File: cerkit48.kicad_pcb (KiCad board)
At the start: 2 copper layers, 251.5 x 128.3 mm, 104 parts, among them J1 I2C, SW1 SW_Push_Dual_x2, SW10 CherryMX, SW11 CherryMX, SW12 CherryMX, SW13 CherryMX, SW14 CherryMX, SW15 CherryMX, SW16 CherryMX, SW17 CherryMX, SW18 CherryMX, SW19 CherryMX, SW2 CherryMX, SW20 CherryMX, SW21 CherryMX, SW22 CherryMX, SW23 CherryMX, SW24 CherryMX, SW25 CherryMX, SW26 CherryMX, SW27 CherryMX, SW28 CherryMX, SW29 CherryMX, SW3 CherryMX, SW30 CherryMX, SW31 CherryMX, SW32 CherryMX, SW33 CherryMX, SW34 CherryMX, SW35 CherryMX, SW36 CherryMX, SW37 CherryMX, SW38 CherryMX, SW39 CherryMX, SW4 CherryMX, SW40 CherryMX, SW41 CherryMX, SW42 CherryMX, SW43 CherryMX, SW44 CherryMX, SW45 CherryMX, SW46 CherryMX, SW47 CherryMX, SW48 CherryMX, SW49 CherryMX, SW5 CherryMX, SW6 CherryMX, SW7 CherryMX, SW8 CherryMX, SW9 CherryMX, U1 proton_c

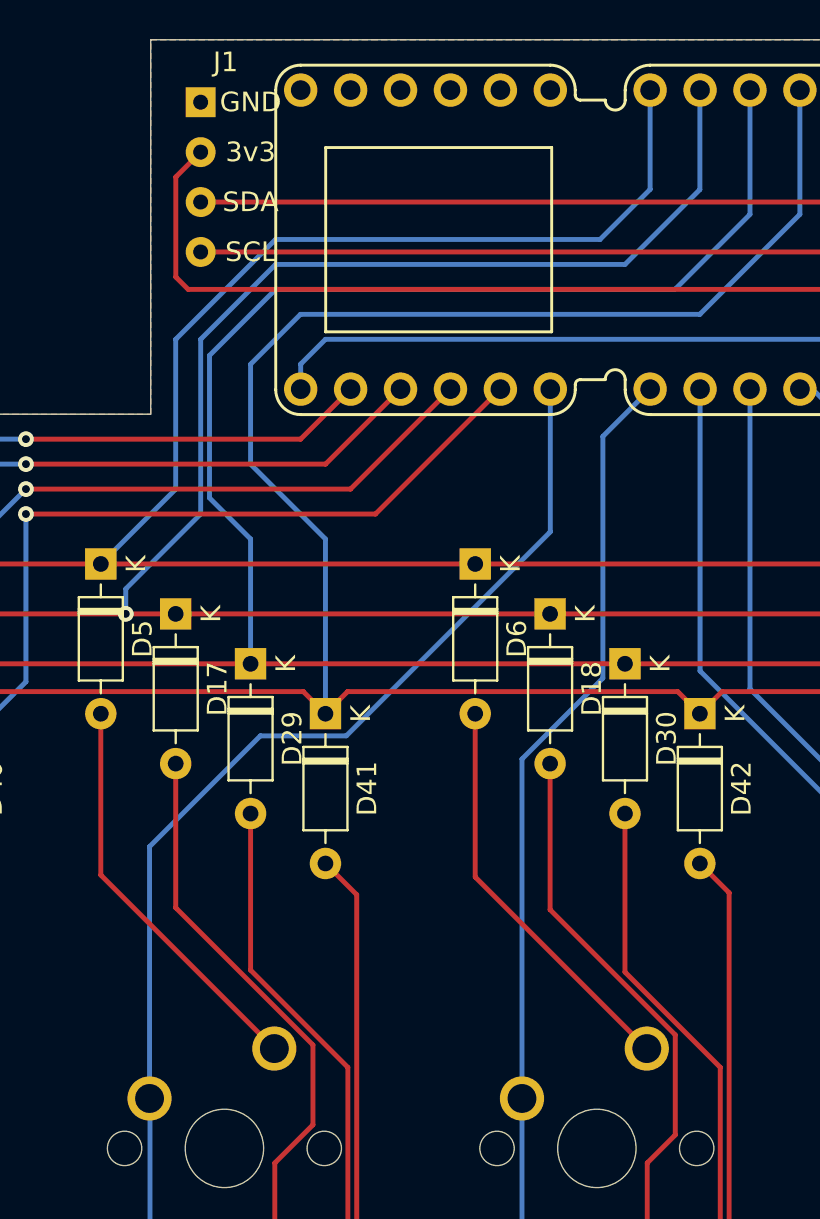
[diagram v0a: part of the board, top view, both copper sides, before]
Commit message: reworked back traces
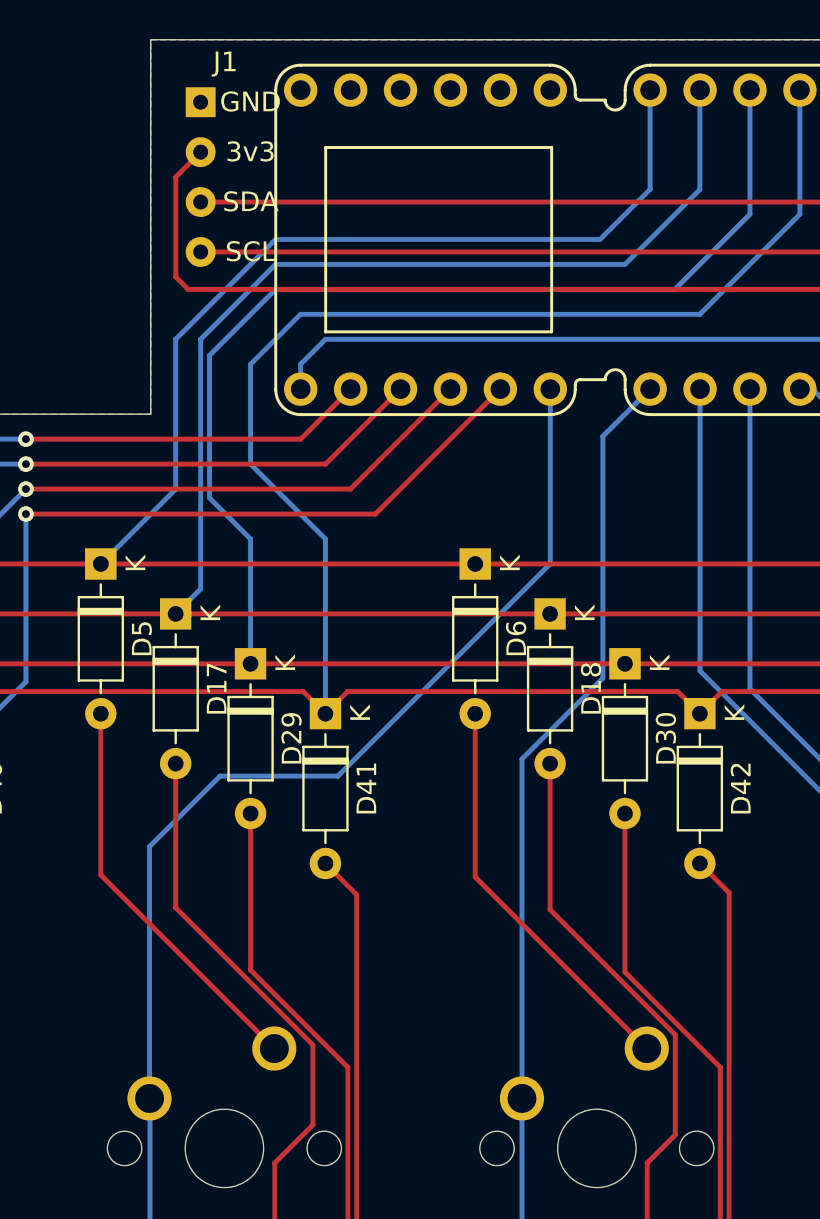
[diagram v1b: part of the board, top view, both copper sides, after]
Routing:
- net ROW1: track 258.7 -> 257.7 mm, vias 1 -> 0
- net COL4: track 104.3 -> 105.3 mm
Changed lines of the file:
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@@
     (thickness 1.6)
     (drawings 1054)
-    (tracks 478)
+    (tracks 475)
     (zones 0)
     (modules 104)
@@
   (segment (start 57.15 60.96) (end 36.83 60.96) (width 0.25) (layer F.Cu) (net 15))
   (segment (start 111.76 60.96) (end 95.25 60.96) (width 0.25) (layer F.Cu) (net 15))
-  (via (at 111.76 60.96) (size 0.8) (drill 0.4) (layers F.Cu B.Cu) (net 15))
-  (segment (start 114.3 57.15) (end 114.3 57.15) (width 0.25) (layer B.Cu) (net 15))
-  (segment (start 140.97 34.32) (end 140.98 34.31) (width 0.25) (layer B.Cu) (net 15))
-  (segment (start 140.97 39.37) (end 140.97 34.32) (width 0.25) (layer B.Cu) (net 15))
-  (segment (start 137.16 43.18) (end 140.97 39.37) (width 0.25) (layer B.Cu) (net 15))
-  (segment (start 111.76 59.69) (end 115.57 55.88) (width 0.25) (layer B.Cu) (net 15))
-  (segment (start 115.57 55.88) (end 115.57 46.99) (width 0.25) (layer B.Cu) (net 15))
-  (segment (start 111.76 60.96) (end 111.76 59.69) (width 0.25) (layer B.Cu) (net 15))
-  (segment (start 115.57 46.99) (end 119.38 43.18) (width 0.25) (layer B.Cu) (net 15))
-  (segment (start 119.38 43.18) (end 137.16 43.18) (width 0.25) (layer B.Cu) (net 15))
+  (segment (start 115.57 59.69) (end 114.3 60.96) (width 0.25) (layer B.Cu) (net 15))
+  (segment (start 115.57 46.99) (end 115.57 59.69) (width 0.25) (layer B.Cu) (net 15))
+  (segment (start 140.97 34.32) (end 140.97 39.37) (width 0.25) (layer B.Cu) (net 15))
+  (segment (start 140.98 34.31) (end 140.97 34.32) (width 0.25) (layer B.Cu) (net 15))
+  (segment (start 140.97 39.37) (end 137.16 43.18) (width 0.25) (layer B.Cu) (net 15))
+  (segment (start 137.16 43.18) (end 119.38 43.18) (width 0.25) (layer B.Cu) (net 15))
+  (segment (start 119.38 43.18) (end 115.57 46.99) (width 0.25) (layer B.Cu) (net 15))
   (segment (start 62.055655 102.033073) (end 62.055655 85.264345) (width 0.25) (layer F.Cu) (net 16))
   (segment (start 62.055655 85.264345) (end 63.5 83.82) (width 0.25) (layer F.Cu) (net 16))
@@
   (segment (start 112.948698 142.633493) (end 112.83523 142.746961) (width 0.25) (layer B.Cu) (net 62))
   (segment (start 112.948698 123.717779) (end 112.948698 142.633493) (width 0.25) (layer B.Cu) (net 62))
-  (segment (start 133.36 56.785002) (end 133.36 49.525) (width 0.25) (layer B.Cu) (net 62))
-  (segment (start 122.980001 67.165001) (end 133.36 56.785002) (width 0.25) (layer B.Cu) (net 62))
-  (segment (start 112.969212 72.805786) (end 118.609997 67.165001) (width 0.25) (layer B.Cu) (net 62))
-  (segment (start 118.609997 67.165001) (end 122.980001 67.165001) (width 0.25) (layer B.Cu) (net 62))
-  (segment (start 112.969212 85.617632) (end 112.969212 72.805786) (width 0.25) (layer B.Cu) (net 62))
+  (segment (start 112.969212 72.805786) (end 112.969212 85.617632) (width 0.25) (layer B.Cu) (net 62))
+  (segment (start 116.559998 69.215) (end 112.969212 72.805786) (width 0.25) (layer B.Cu) (net 62))
+  (segment (start 122.555 69.215) (end 116.559998 69.215) (width 0.25) (layer B.Cu) (net 62))
+  (segment (start 133.36 49.525) (end 133.36 58.41) (width 0.25) (layer B.Cu) (net 62))
+  (segment (start 133.36 58.41) (end 122.555 69.215) (width 0.25) (layer B.Cu) (net 62))
   (segment (start 131.957876 123.71475) (end 132.010576 123.66205) (width 0.25) (layer B.Cu) (net 63))
   (segment (start 131.957876 142.76019) (end 131.957876 123.71475) (width 0.25) (layer B.Cu) (net 63))

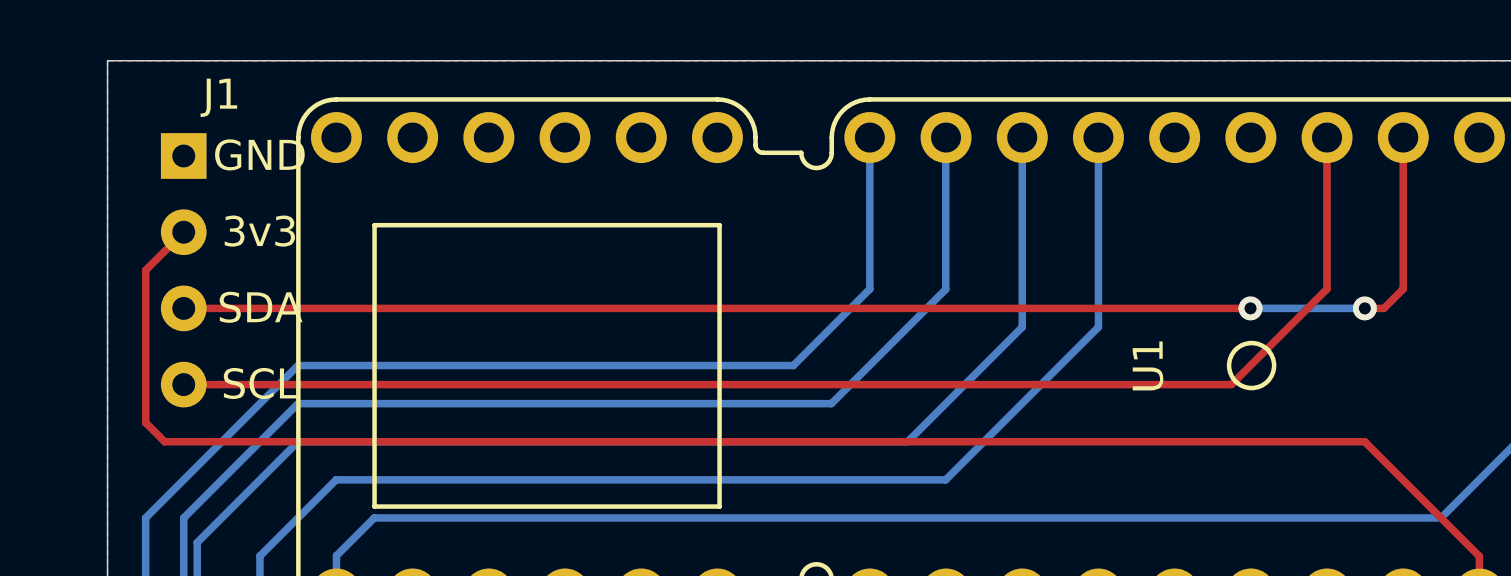
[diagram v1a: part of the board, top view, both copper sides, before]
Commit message: reworked front traces
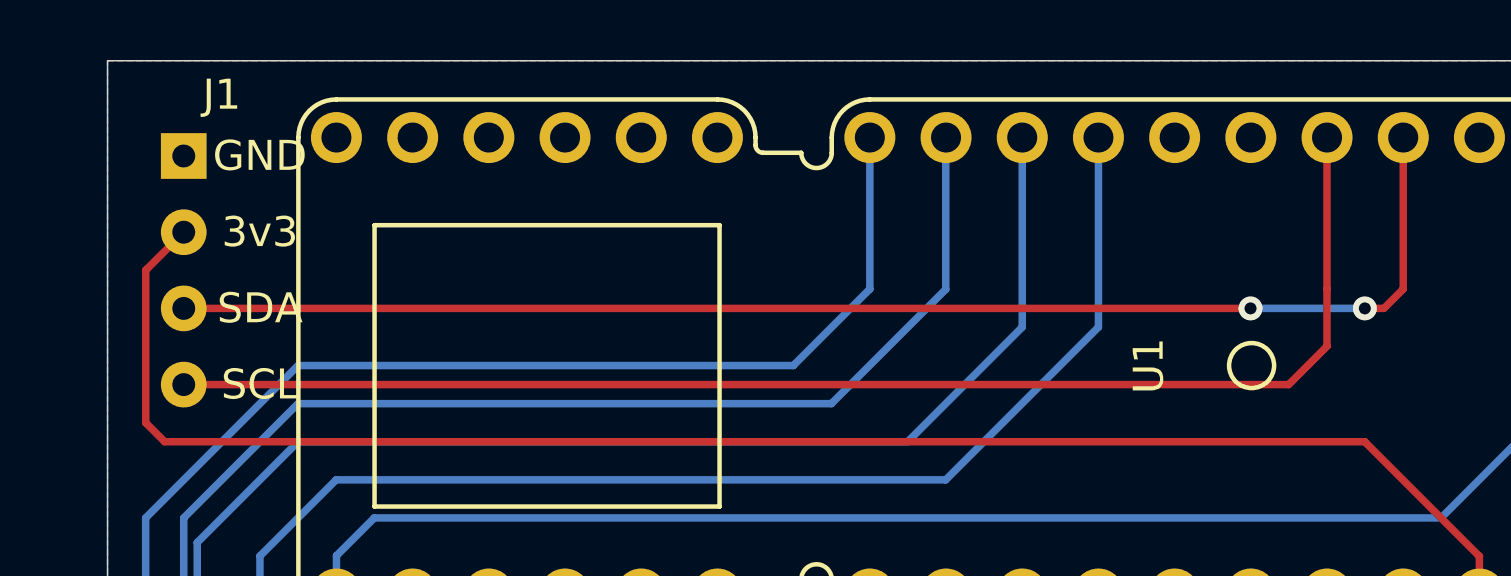
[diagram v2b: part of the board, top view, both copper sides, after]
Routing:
- net SCL: track 44.5 -> 45.6 mm
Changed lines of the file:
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@@
     (thickness 1.6)
     (drawings 1054)
-    (tracks 475)
+    (tracks 476)
     (zones 0)
     (modules 104)
@@
   (page A4)
   (layers
-    (0 F.Cu signal hide)
-    (31 B.Cu signal)
+    (0 F.Cu signal)
+    (31 B.Cu signal hide)
     (32 B.Adhes user hide)
     (33 F.Adhes user hide)
@@
   (segment (start 256.867319 135.878264) (end 252.557254 140.188329) (width 0.25) (layer F.Cu) (net 52))
   (segment (start 254 73.66) (end 256.867319 76.527319) (width 0.25) (layer F.Cu) (net 52))
-  (segment (start 153.68 34.31) (end 153.68 39.36) (width 0.25) (layer F.Cu) (net 53))
-  (segment (start 150.495 42.545) (end 115.57 42.545) (width 0.25) (layer F.Cu) (net 53))
-  (segment (start 153.68 39.36) (end 150.495 42.545) (width 0.25) (layer F.Cu) (net 53))
+  (segment (start 153.68 39.36) (end 153.68 34.31) (width 0.25) (layer F.Cu) (net 53))
+  (segment (start 153.68 41.265) (end 153.68 39.36) (width 0.25) (layer F.Cu) (net 53))
+  (segment (start 115.57 42.545) (end 152.4 42.545) (width 0.25) (layer F.Cu) (net 53))
+  (segment (start 152.4 42.545) (end 153.68 41.265) (width 0.25) (layer F.Cu) (net 53))
   (via (at 154.94 40.005) (size 0.8) (drill 0.4) (layers F.Cu B.Cu) (net 54))
   (segment (start 115.57 40.005) (end 151.13 40.005) (width 0.25) (layer F.Cu) (net 54))
@@
   (segment (start 210.424998 53.34) (end 242.650747 85.565749) (width 0.25) (layer B.Cu) (net 69))
   (segment (start 160.02 53.34) (end 210.424998 53.34) (width 0.25) (layer B.Cu) (net 69))
-  (zone (net 56) (net_name GND) (layer F.Cu) (hatch edge 0.508)
+  (zone (net 56) (net_name GND) (layer B.Cu) (hatch edge 0.508)
     (connect_pads (clearance 0.508))
     (min_thickness 0.254)
@@
     )
   )
-  (zone (net 56) (net_name GND) (layer B.Cu) (hatch edge 0.508)
+  (zone (net 56) (net_name GND) (layer F.Cu) (hatch edge 0.508)
     (connect_pads (clearance 0.508))
     (min_thickness 0.254)

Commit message: shrank the board size
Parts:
- moved SW1 9.69 mm to (255.3, 57.8), turned to 180 degrees
- moved H4 9.38 mm to (31.1, 151.8)
- moved H1 8.25 mm to (31.1, 54.6)
- moved H5 6.75 mm to (261.6, 151.8)
- moved H2 5.08 mm to (261.6, 54.6)
- moved D1 2.54 mm to (35.6, 58.4)
- moved D13 2.54 mm to (39.4, 61.0)
- moved D25 2.54 mm to (43.2, 63.5)
- moved D37 2.54 mm to (47.0, 66.0)
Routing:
- net Net-(SW1-Pad2): track 168.4 -> 142.9 mm
- net ROW3: track 276.6 -> 272.5 mm
- net ROW2: track 262.9 -> 260.4 mm
- net ROW0: track 254.9 -> 252.4 mm
- net ROW1: track 257.7 -> 255.1 mm
- net Net-(D13-Pad2): track 37.2 -> 36.1 mm
- net Net-(D37-Pad2): track 69.3 -> 68.3 mm
- net Net-(D1-Pad2): track 21.2 -> 20.1 mm
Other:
- board size 251.5 x 128.3 mm -> 238.1 x 123.8 mm

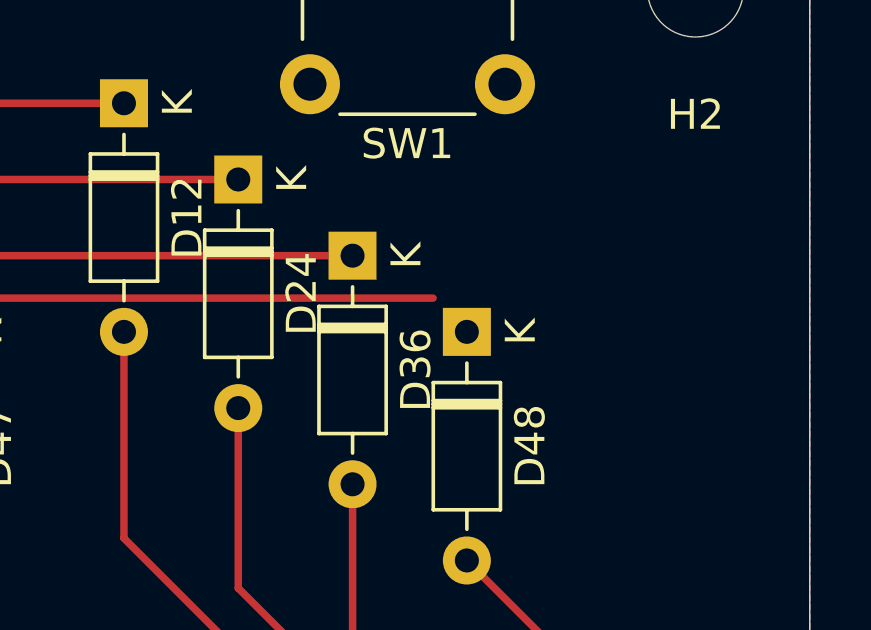
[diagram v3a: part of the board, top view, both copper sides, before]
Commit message: fixed unconnected diode
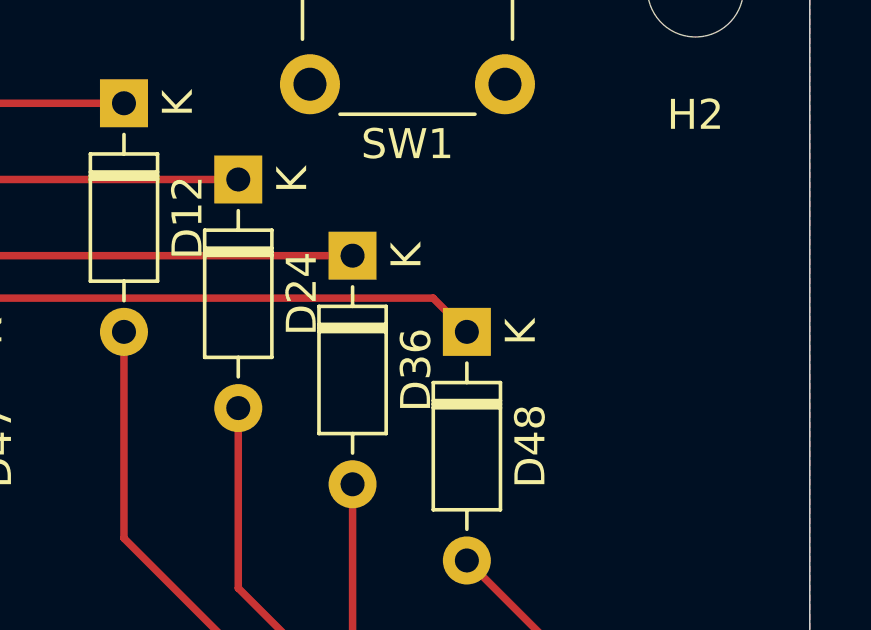
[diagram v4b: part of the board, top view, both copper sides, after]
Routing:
- net ROW3: track 272.5 -> 274.1 mm
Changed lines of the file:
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@@
     (thickness 1.6)
     (drawings 1053)
-    (tracks 471)
+    (tracks 472)
     (zones 0)
     (modules 104)
@@
   (layers
     (0 F.Cu signal)
-    (31 B.Cu signal)
+    (31 B.Cu signal hide)
     (32 B.Adhes user hide)
     (33 F.Adhes user hide)
@@
     (35 F.Paste user hide)
     (36 B.SilkS user hide)
-    (37 F.SilkS user hide)
+    (37 F.SilkS user)
     (38 B.Mask user hide)
     (39 F.Mask user hide)
@@
     (45 Margin user hide)
     (46 B.CrtYd user hide)
-    (47 F.CrtYd user)
+    (47 F.CrtYd user hide)
     (48 B.Fab user hide)
     (49 F.Fab user hide)
@@
   (segment (start 48.115001 64.914999) (end 63.644999 64.914999) (width 0.25) (layer F.Cu) (net 41))
   (segment (start 46.99 66.04) (end 48.115001 64.914999) (width 0.25) (layer F.Cu) (net 41))
+  (segment (start 254 66.04) (end 252.874999 64.914999) (width 0.25) (layer F.Cu) (net 41))
   (segment (start 66.04 74.93) (end 64.77 73.66) (width 0.25) (layer F.Cu) (net 42))
   (segment (start 66.208356 119.20716) (end 66.208356 75.098356) (width 0.25) (layer F.Cu) (net 42))

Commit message: reworked diodes so the board could be smaller
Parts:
- removed SW1: SW_Push_Dual_x2, Button_Switch_THT:SW_PUSH_6mm
- moved D48 58.8 mm to (260.4, 124.5), turned to 90 degrees
- moved D38 58.6 mm to (69.8, 124.5), turned to 90 degrees
- moved D39 58.6 mm to (88.9, 124.5), turned to 90 degrees
- moved D40 58.6 mm to (108.0, 124.5), turned to 90 degrees
- moved D41 58.6 mm to (127.0, 124.5), turned to 90 degrees
- moved D42 58.6 mm to (146.1, 124.5), turned to 90 degrees
- moved D44 58.6 mm to (184.2, 124.5), turned to 90 degrees
- moved D46 58.6 mm to (222.2, 124.5), turned to 90 degrees
- moved D47 58.6 mm to (241.3, 124.5), turned to 90 degrees
- moved D43 58.6 mm to (165.1, 124.5), turned to 90 degrees
- moved D45 58.6 mm to (203.2, 124.5), turned to 90 degrees
- moved D37 58.5 mm to (50.8, 124.5), turned to 90 degrees
- moved D36 43.1 mm to (260.4, 105.4), turned to 90 degrees
- moved D31 43.0 mm to (165.7, 105.4), turned to 90 degrees
- moved D26 42.8 mm to (69.8, 105.4), turned to 90 degrees
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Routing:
- net Net-(U1-PadRST): track 142.9 -> 0.00 mm
- net ROW3: track 274.1 -> 349.2 mm, vias 0 -> 3
- net Net-(D48-Pad2): track 69.5 -> 7.22 mm
- net Net-(D46-Pad2): track 69.0 -> 7.22 mm
- net Net-(D47-Pad2): track 69.0 -> 7.22 mm
- net Net-(D43-Pad2): track 69.0 -> 7.24 mm
- net Net-(D41-Pad2): track 69.0 -> 7.23 mm
- net Net-(D42-Pad2): track 68.9 -> 7.15 mm
- net Net-(D45-Pad2): track 68.9 -> 7.20 mm
- net Net-(D40-Pad2): track 68.9 -> 7.24 mm
- net Net-(D44-Pad2): track 68.9 -> 7.19 mm
- net Net-(D38-Pad2): track 68.9 -> 7.21 mm
- net Net-(D39-Pad2): track 68.6 -> 7.22 mm
- net Net-(D37-Pad2): track 68.3 -> 7.22 mm
- net ROW2: track 260.4 -> 309.8 mm, vias 0 -> 3
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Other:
- board size 238.1 x 123.8 mm -> 237.5 x 104.1 mm

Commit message: Move Proton to bottom of board and made board smaller
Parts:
- U1: footprint proton_c:proton_c -> cerkit48:proton_c_no_center_pins
- moved J1 98.3 mm to (212.7, 54.0), turned to 270 degrees
- moved U1 90.8 mm to (218.4, 102.9), turned to 90 degrees
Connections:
- U1 pad A0: COL10 -> COL2
- U1 pad A1: COL11 -> COL1
- U1 pad A13: COL0 -> Net-(U1-PadA13)
- U1 pad A14: COL1 -> COL11
- U1 pad A2: Net-(U1-PadA2) -> COL0
- U1 pad B0: ROW0 -> ROW3
- U1 pad B1: ROW1 -> ROW2
- U1 pad B10: COL4 -> COL8
- U1 pad B11: COL3 -> COL9
- U1 pad B12: COL2 -> COL10
- U1 pad B13: COL8 -> COL4
- U1 pad B14: COL7 -> COL5
- U1 pad B2: ROW2 -> ROW1
- U1 pad B3: ROW3 -> ROW0
- U1 pad B8: COL9 -> COL3
- U1 pad B9: COL5 -> COL7
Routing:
- net ROW3: track 349.2 -> 227.8 mm, vias 3 -> 0
- net COL4: track 82.2 -> 195.3 mm, vias 0 -> 2
- net COL0: track 149.3 -> 258.3 mm, vias 0 -> 2
- net ROW2: track 309.8 -> 215.5 mm, vias 3 -> 1
- net COL11: track 155.7 -> 62.2 mm
- net COL2: track 116.6 -> 205.6 mm, vias 0 -> 2
- net COL3: track 101.9 -> 190.3 mm, vias 0 -> 2
- net COL1: track 134.2 -> 222.4 mm, vias 0 -> 2
- net COL5: track 72.2 -> 154.1 mm
- net COL10: track 139.6 -> 74.6 mm
- net COL6: track 74.3 -> 135.5 mm, vias 0 -> 1
- net ROW1: track 290.2 -> 235.2 mm
- net SCL: track 45.6 -> 96.9 mm, vias 0 -> 2
- net SDA: track 46.0 -> 84.2 mm
- net COL7: track 89.6 -> 118.8 mm, vias 0 -> 1
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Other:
- board size 237.5 x 104.1 mm -> 237.5 x 85.1 mm

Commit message: flipped Proton so it will be arranged correctly on the back of the board.
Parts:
- U1: moved to B.Cu
- turned U1 to 270 degrees
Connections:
- U1 pad A0: COL2 -> Net-(U1-PadA0)
- U1 pad A1: COL1 -> Net-(U1-PadA1)
- U1 pad A14: COL11 -> Net-(U1-PadA14)
- U1 pad A15: Net-(U1-PadA15) -> COL11
- U1 pad A2: COL0 -> Net-(U1-PadA2)
- U1 pad A6: Net-(U1-PadA6) -> COL8
- U1 pad A7: Net-(U1-PadA7) -> COL9
- U1 pad A8: Net-(U1-PadA8) -> COL10
- U1 pad B0: ROW3 -> COL7
- U1 pad B1: ROW2 -> COL6
- U1 pad B10: COL8 -> ROW3
- U1 pad B11: COL9 -> Net-(U1-PadB11)
- U1 pad B12: COL10 -> Net-(U1-PadB12)
- U1 pad B13: COL4 -> ROW0
- U1 pad B14: COL5 -> ROW1
- U1 pad B15: COL6 -> ROW2
- U1 pad B2: ROW1 -> COL5
- U1 pad B3: ROW0 -> COL4
- U1 pad B4: Net-(U1-PadB4) -> COL3
- U1 pad B5: Net-(U1-PadB5) -> COL2
- U1 pad B6: SCL -> COL1
- U1 pad B7: SDA -> COL0
- U1 pad B8: COL3 -> SCL
- U1 pad B9: COL7 -> SDA
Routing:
- net 3.3V: track 43.9 -> 72.3 mm, vias 0 -> 1
- net SDA: track 84.2 -> 101.9 mm, vias 2 -> 1
- net COL10: track 74.6 -> 86.1 mm
- net SCL: track 96.9 -> 103.7 mm
- net COL9: track 95.1 -> 100.4 mm
- net COL8: track 106.0 -> 110.0 mm
- net COL0: track 258.3 -> 256.0 mm
- net COL11: track 62.2 -> 61.2 mm
- net ROW3: track 227.8 -> 226.8 mm
- net ROW1: track 235.2 -> 234.7 mm

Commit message: Updated reame and fixed stray trace in PCB
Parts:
- moved D11 4.45 mm to (236.9, 67.3)
- moved D12 4.45 mm to (255.9, 67.3)
- moved D18 4.45 mm to (141.6, 86.4)
- moved D23 4.45 mm to (236.9, 86.4)
- moved D24 4.45 mm to (255.9, 86.4)
- moved D30 4.45 mm to (141.6, 105.4)
- moved D31 4.45 mm to (161.3, 105.4)
- moved D35 4.45 mm to (236.9, 105.4)
- moved D36 4.45 mm to (255.9, 105.4)
- moved D42 4.45 mm to (141.6, 124.5)
- moved D47 4.45 mm to (236.9, 124.5)
- moved D48 4.45 mm to (255.9, 124.5)
- moved D6 4.45 mm to (141.6, 67.3)
- moved H3 4.45 mm to (141.6, 92.7)
- moved H5 4.45 mm to (255.9, 132.1)
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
